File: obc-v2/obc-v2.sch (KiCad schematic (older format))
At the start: 15 parts

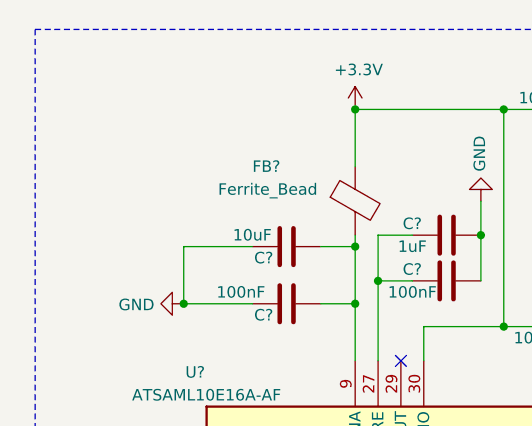
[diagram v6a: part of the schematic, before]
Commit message: obc-v2: Add reset button
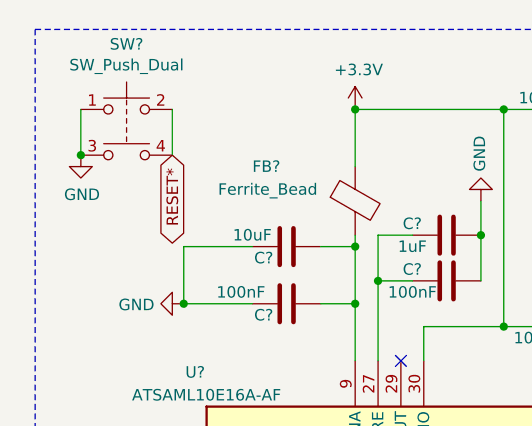
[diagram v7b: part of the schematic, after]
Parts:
- added SW?: SW_Push_Dual, symbol Switch:SW_Push_Dual
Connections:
- net GND: now also SW?.1, SW?.3
- net RESET*: now also SW?.2, SW?.4
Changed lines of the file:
@@
 Text Notes 5500 4900 0    50   ~ 0
 1-wire Interface
+$Comp
+L Switch:SW_Push_Dual SW?
+U 1 1 612A144F
+P 1600 1150
+F 0 "SW?" H 1600 1435 50  0000 C CNN
+F 1 "SW_Push_Dual" H 1600 1344 50  0000 C CNN
+F 2 "" H 1600 1350 50  0001 C CNN
+F 3 "~" H 1600 1350 50  0001 C CNN
+	1    1600 1150
+	1    0    0    -1
+$EndComp
+Text GLabel 1800 1350 3    50   BiDi ~ 0
+RESET*
+$Comp
+L power:GND #PWR?
+U 1 1 61309369
+P 1400 1350
+F 0 "#PWR?" H 1400 1100 50  0001 C CNN
+F 1 "GND" H 1405 1177 50  0000 C CNN
+F 2 "" H 1400 1350 50  0001 C CNN
+F 3 "" H 1400 1350 50  0001 C CNN
+	1    1400 1350
+	1    0    0    -1
+$EndComp
+Wire Wire Line
+	1400 1150 1400 1350
+Connection ~ 1400 1350
+Wire Wire Line
+	1800 1150 1800 1350
 $EndSCHEMATC

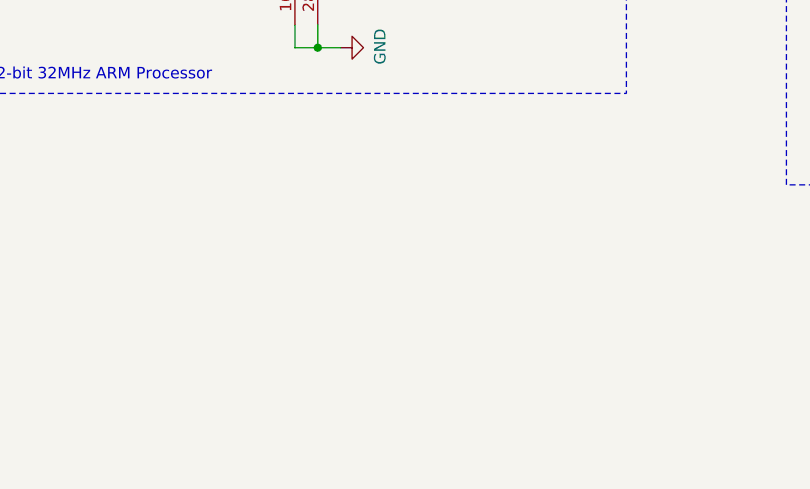
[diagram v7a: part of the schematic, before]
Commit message: obc-v2: Add voltage regulator
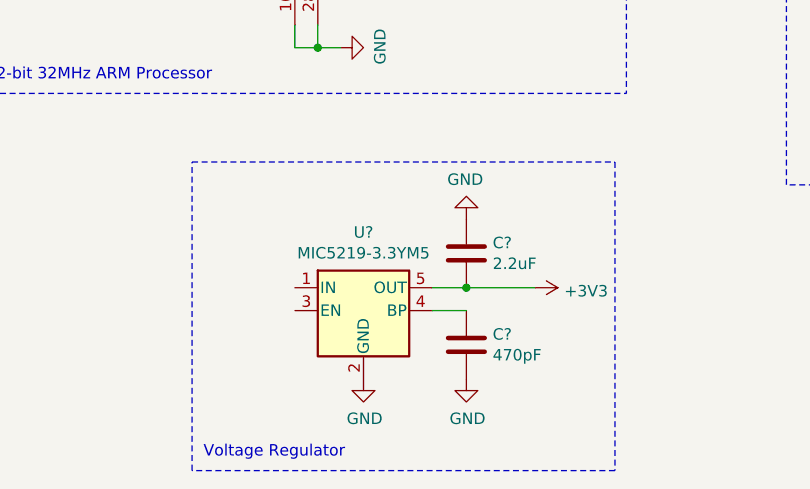
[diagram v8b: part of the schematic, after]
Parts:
- added C?: 2.2uF, symbol Device:C
- added C?: 470pF, symbol Device:C
- added U?: MIC5219-3.3YM5, Package_TO_SOT_SMD:SOT-23-5, symbol Regulator_Linear:MIC5219-3.3YM5
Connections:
- net +3V3: now also C?.1, U?.5 (OUT)
- net GND: now also C?.2, C?.2, U?.2 (GND)
- new net: C?.1, U?.4 (BP)
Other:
- note added: "Voltage Regulator"
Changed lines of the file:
@@
 Wire Wire Line
 	1800 1150 1800 1350
+$Comp
+L Regulator_Linear:MIC5219-3.3YM5 U?
+U 1 1 6130CF2C
+P 3000 5500
+F 0 "U?" H 3000 5842 50  0000 C CNN
+F 1 "MIC5219-3.3YM5" H 3000 5751 50  0000 C CNN
+F 2 "Package_TO_SOT_SMD:SOT-23-5" H 3000 5825 50  0001 C CNN
+F 3 "http://ww1.microchip.com/downloads/en/DeviceDoc/MIC5219-500mA-Peak-Output-LDO-Regulator-DS20006021A.pdf" H 3000 5500 50  0001 C CNN
+	1    3000 5500
+	1    0    0    -1
+$EndComp
+$Comp
+L power:GND #PWR?
+U 1 1 6130E43E
+P 3000 5800
+F 0 "#PWR?" H 3000 5550 50  0001 C CNN
+F 1 "GND" H 3005 5627 50  0000 C CNN
+F 2 "" H 3000 5800 50  0001 C CNN
+F 3 "" H 3000 5800 50  0001 C CNN
+	1    3000 5800
+	1    0    0    -1
+$EndComp
+$Comp
+L power:+3V3 #PWR?
+U 1 1 6130EAA8
+P 3750 5400
+F 0 "#PWR?" H 3750 5250 50  0001 C CNN
+F 1 "+3V3" V 3765 5528 50  0000 L CNN
+F 2 "" H 3750 5400 50  0001 C CNN
+F 3 "" H 3750 5400 50  0001 C CNN
+	1    3750 5400
+	0    1    1    0
+$EndComp
+$Comp
+L Device:C C?
+U 1 1 6130FC01
+P 3450 5250
+F 0 "C?" H 3335 5204 50  0000 R CNN
+F 1 "2.2uF" H 3335 5295 50  0000 R CNN
+F 2 "" H 3488 5100 50  0001 C CNN
+F 3 "~" H 3450 5250 50  0001 C CNN
+	1    3450 5250
+	-1   0    0    1
+$EndComp
+Wire Wire Line
+	3300 5400 3450 5400
+$Comp
+L power:GND #PWR?
+U 1 1 61312359
+P 3450 5100
+F 0 "#PWR?" H 3450 4850 50  0001 C CNN
+F 1 "GND" H 3455 4927 50  0000 C CNN
+F 2 "" H 3450 5100 50  0001 C CNN
+F 3 "" H 3450 5100 50  0001 C CNN
+	1    3450 5100
+	-1   0    0    1
+$EndComp
+Wire Wire Line
+	3450 5400 3750 5400
+Connection ~ 3450 5400
+$Comp
+L Device:C C?
+U 1 1 61313A92
+P 3450 5650
+F 0 "C?" H 3565 5696 50  0000 L CNN
+F 1 "470pF" H 3565 5605 50  0000 L CNN
+F 2 "" H 3488 5500 50  0001 C CNN
+F 3 "~" H 3450 5650 50  0001 C CNN
+	1    3450 5650
+	1    0    0    -1
+$EndComp
+$Comp
+L power:GND #PWR?
+U 1 1 613140DB
+P 3450 5800
+F 0 "#PWR?" H 3450 5550 50  0001 C CNN
+F 1 "GND" H 3455 5627 50  0000 C CNN
+F 2 "" H 3450 5800 50  0001 C CNN
+F 3 "" H 3450 5800 50  0001 C CNN
+	1    3450 5800
+	1    0    0    -1
+$EndComp
+Wire Wire Line
+	3300 5500 3450 5500
+Wire Notes Line
+	2250 4850 4100 4850
+Wire Notes Line
+	4100 4850 4100 6200
+Wire Notes Line
+	4100 6200 2250 6200
+Wire Notes Line
+	2250 6200 2250 4850
+Text Notes 2300 6150 0    50   ~ 0
+Voltage Regulator
 $EndSCHEMATC
